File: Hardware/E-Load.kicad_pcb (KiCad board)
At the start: 2 copper layers, 63.5 x 71.1 mm, 53 parts, among them J1 Barrel_Jack, J2 Conn_01x05_Male, J3 Conn_01x08_Male, J4 Screw_Terminal_01x03, Q1 BUK7M45-40EX, SW1 SW_SPST, SW2 SW_Push, SW3 SW_Push, SW4 SW_Push, U1 AP2210K-3.3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

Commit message: Update E-Load.kicad_pcb
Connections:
- U4 pad 6: Net-(D2-Pad1) -> /CurrentControl/ADC
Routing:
- net /CurrentControl/ADC: track 16.6 -> 25.8 mm

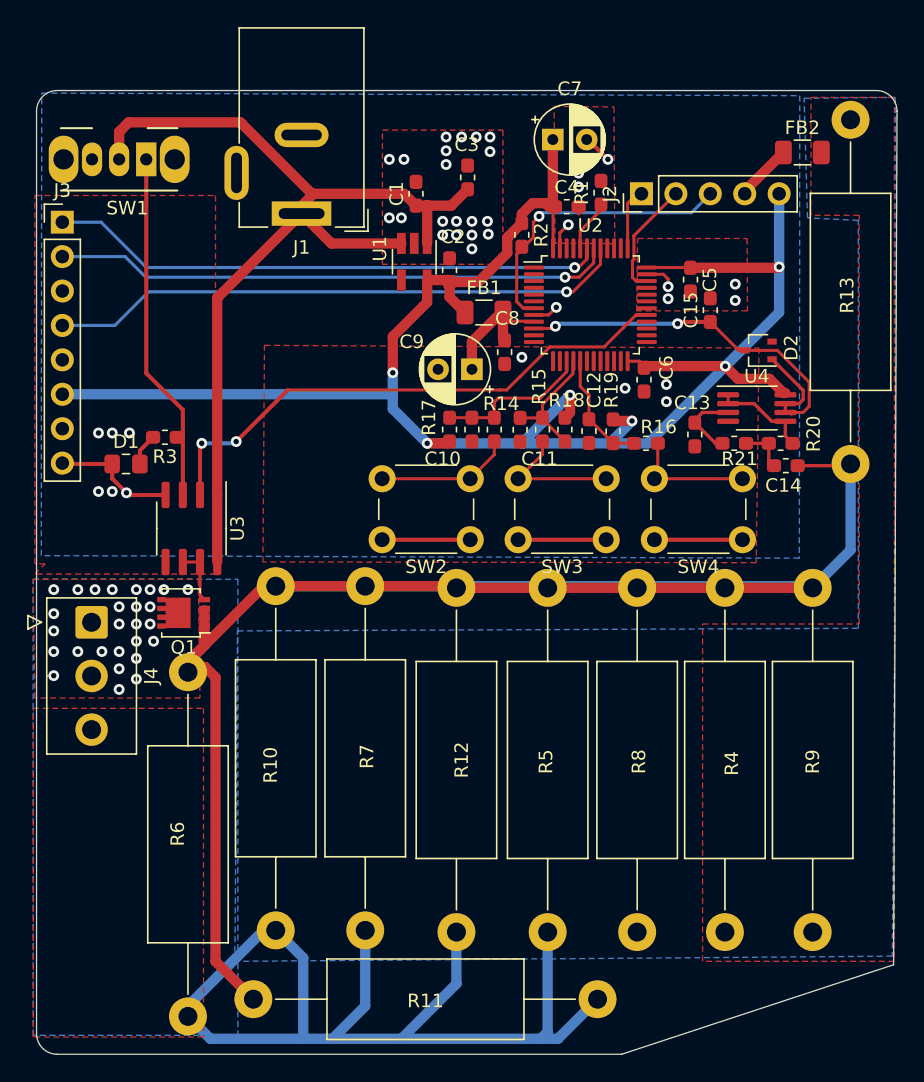
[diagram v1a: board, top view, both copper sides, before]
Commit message: Replaced gate driver with opamp. Replaced feedback circuit with unity gain buffer
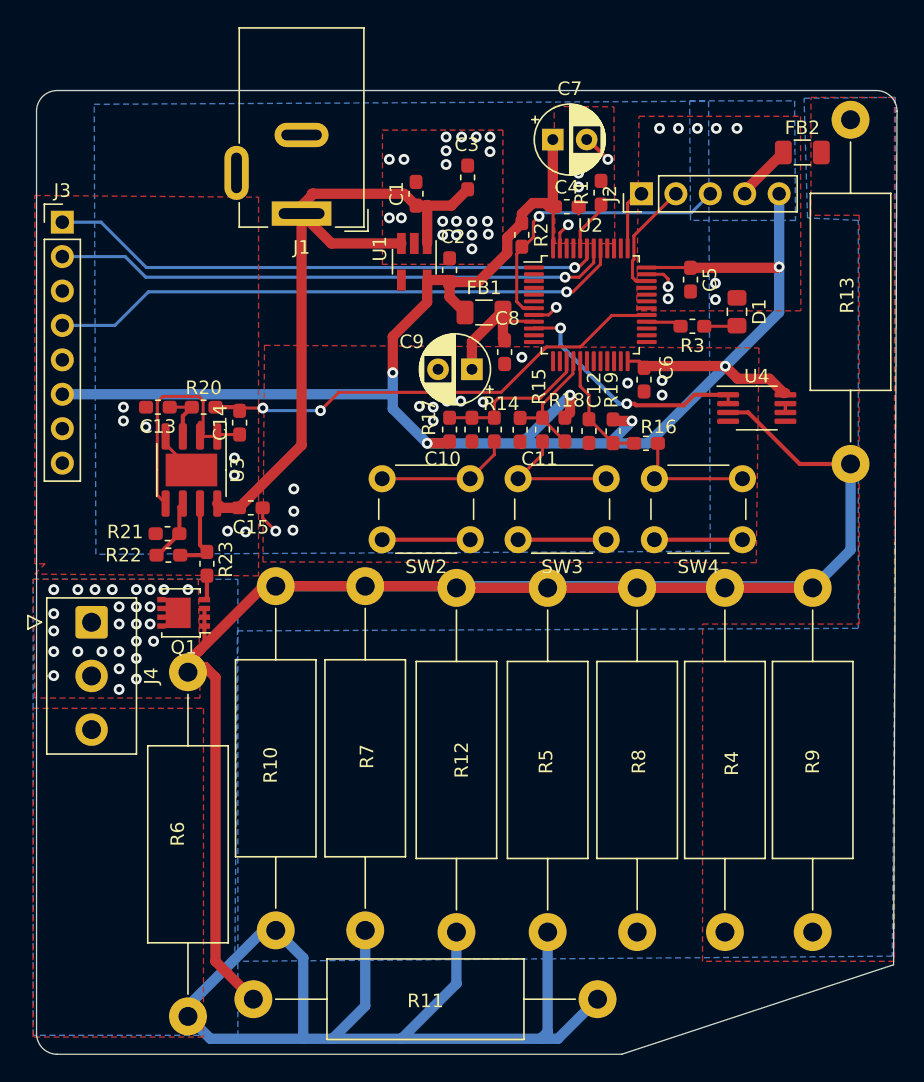
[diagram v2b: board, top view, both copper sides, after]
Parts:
- removed D2: BAT54W, Package_TO_SOT_SMD:SOT-323_SC-70
- removed SW1: SW_SPST, Button_Switch_THT:SW_CuK_OS102011MA1QN1_SPDT_Angled
- added R22: 2.7k, Resistor_SMD:R_0603_1608Metric_Pad1.05x0.95mm_HandSolder, F.Cu at (152.0, 93.7)
- added R23: 15, Resistor_SMD:R_0603_1608Metric_Pad1.05x0.95mm_HandSolder, F.Cu at (154.8, 94.4)
- C15: value 1u -> 100nF
- R20: value 4.32k -> 10.2k
- R21: value 10.2k -> 1k
- R3: value 1K -> 1k
- U3: value MCP14A0302 -> ADA4898-2; footprint Package_SO:SOIC-8_3.9x4.9mm_P1.27mm -> Package_SO:SOIC-8-1EP_3.9x4.9mm_P1.27mm_EP2.41x3.81mm
- moved D1 46.5 mm to (193.9, 75.8), turned to 270 degrees
- moved R20 43.2 mm to (154.6, 82.8)
- moved R21 42.3 mm to (151.9, 92.1)
- moved C14 40.0 mm to (157.2, 83.9), turned to 90 degrees
- moved R3 39.8 mm to (190.6, 76.8)
- moved C13 39.7 mm to (151.2, 82.8), turned to 180 degrees
- moved C15 36.9 mm to (158.1, 90.2), turned to 180 degrees
- moved U3 4.32 mm to (153.7, 87.4)
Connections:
- C14 pad 2: Net-(C14-Pad2) -> /CurrentControl/PWM
- C15 pad 1: /CurrentControl/ADC -> GND
- C15 pad 2: GND -> +12V
- R20 pad 1: Net-(C14-Pad2) -> Net-(C13-Pad1)
- R20 pad 2: /CurrentControl/Vmeas -> /CurrentControl/PWM
- R21 pad 1: Net-(C13-Pad1) -> GND
- R21 pad 2: Net-(C14-Pad2) -> Net-(R21-Pad2)
- R3 pad 1: Net-(R3-Pad1) -> Net-(D1-Pad2)
- R3 pad 2: Net-(D1-Pad2) -> Net-(R3-Pad2)
- U2 pad 28: (no net) -> Net-(R3-Pad2)
- U3 pad 1: +12V -> Net-(C14-Pad1)
- U3 pad 2: /CurrentControl/PWM -> Net-(C14-Pad1)
- U3 pad 3: Net-(R3-Pad1) -> Net-(C13-Pad1)
- U3 pad 5: GND -> Net-(C14-Pad1)
- U3 pad 6: Net-(Q1-Pad4) -> Net-(R21-Pad2)
- U3 pad 7: Net-(Q1-Pad4) -> Net-(R22-Pad1)
- U4 pad 1: Net-(C14-Pad1) -> /CurrentControl/ADC
- U4 pad 2: Net-(C14-Pad1) -> /CurrentControl/ADC
- U4 pad 3: Net-(C13-Pad1) -> /CurrentControl/Vmeas
- U4 pad 5: Net-(C14-Pad1) -> (no net)
- U4 pad 6: /CurrentControl/ADC -> (no net)
- U4 pad 7: Net-(D2-Pad1) -> (no net)
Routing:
- net Net-(R3-Pad1): track 26.4 -> 0.00 mm
- net +12V: track 73.3 -> 51.6 mm
- net Net-(C14-Pad1): track 7.26 -> 18.2 mm
- net /CurrentControl/ADC: track 25.8 -> 18.4 mm
- net Net-(D2-Pad1): track 6.02 -> 0.00 mm
- net Net-(R22-Pad1): track 0.00 -> 5.85 mm
- net /CurrentControl/PWM: track 41.0 -> 35.3 mm
- net /CurrentControl/Vmeas: track 135.4 -> 140.5 mm
- net Net-(R21-Pad2): track 0.00 -> 4.67 mm
- net GND: track 41.8 -> 38.0 mm, vias 39 -> 55
- net Net-(C14-Pad2): track 3.49 -> 0.00 mm
- net Net-(R3-Pad2): track 0.00 -> 2.63 mm
- net Net-(Q1-Pad4): track 4.18 -> 1.84 mm
- net Net-(C13-Pad1): track 5.55 -> 4.06 mm
- net (no net): track 0.00 -> 0.65 mm

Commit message: Changed the PWM control circuit
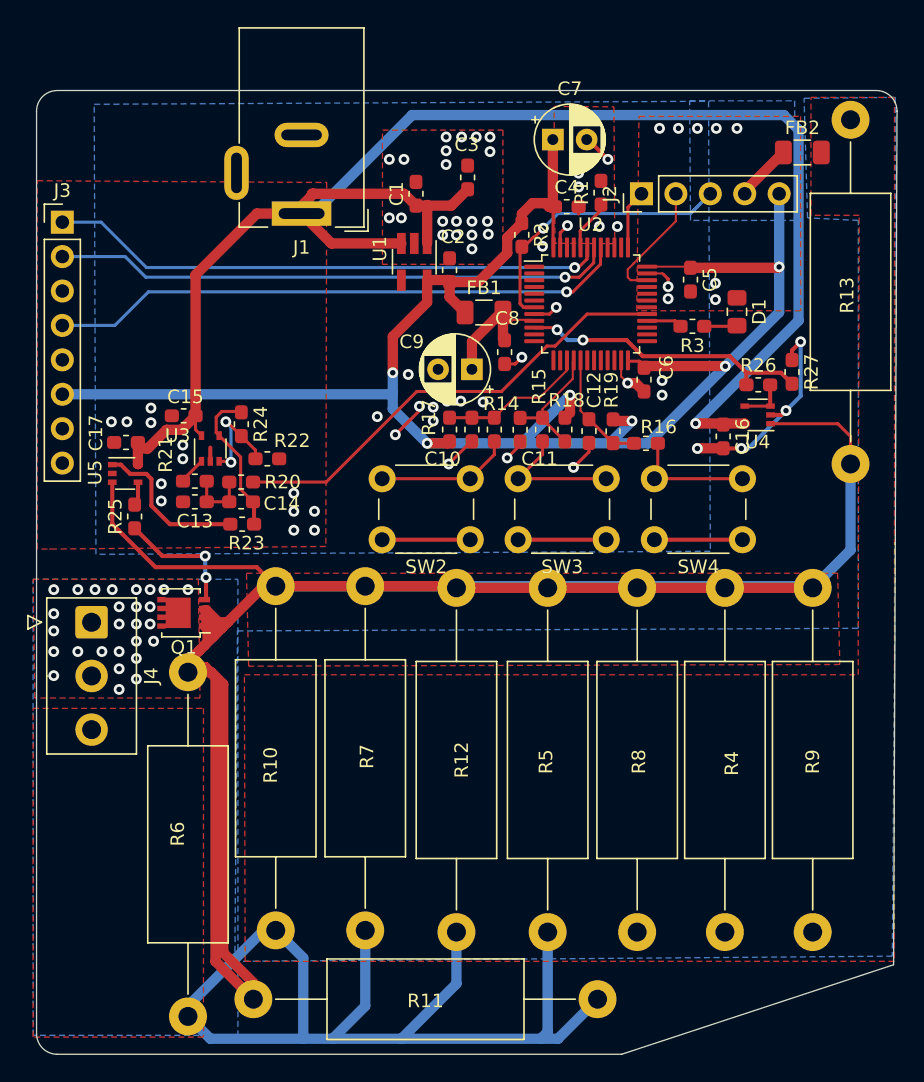
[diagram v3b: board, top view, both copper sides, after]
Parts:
- added C16: 1n, Capacitor_SMD:C_0603_1608Metric_Pad1.05x0.95mm_HandSolder, F.Cu at (192.9, 85.0)
- added C17: 1n, Capacitor_SMD:C_0603_1608Metric_Pad1.05x0.95mm_HandSolder, F.Cu at (148.8, 85.4)
- added R24: 46.4k, Resistor_SMD:R_0603_1608Metric_Pad1.05x0.95mm_HandSolder, F.Cu at (157.4, 84.1)
- added R25: 50, Resistor_SMD:R_0603_1608Metric_Pad1.05x0.95mm_HandSolder, F.Cu at (149.5, 90.9)
- added R26: 20k, Resistor_SMD:R_0603_1608Metric_Pad1.05x0.95mm_HandSolder, F.Cu at (195.5, 81.2)
- added R27: 10k, Resistor_SMD:R_0603_1608Metric_Pad1.05x0.95mm_HandSolder, F.Cu at (198.0, 80.2)
- added U5: TLV172IDCK, Package_TO_SOT_SMD:SOT-353_SC-70-5, F.Cu at (148.8, 87.7)
- C13: value 0.01uF -> 1n
- C14: value 0.082uF -> 470p
- C15: value 100nF -> 1n
- R20: value 10.2k -> 25.5k
- R21: value 1k -> 21k
- R22: value 2.7k -> 23.2k
- R23: value 15 -> 50
- U2: value STM32F102C8Tx -> STM32F103C8Tx
- U3: value ADA4898-2 -> TLV172IDCK; footprint Package_SO:SOIC-8-1EP_3.9x4.9mm_P1.27mm_EP2.41x3.81mm -> Package_TO_SOT_SMD:SOT-353_SC-70-5
- U4: value MCP6L02x-xMS -> TLV172IDCK; footprint Package_SO:MSOP-8_3x3mm_P0.65mm -> Package_TO_SOT_SMD:SOT-353_SC-70-5
- moved R22 10.2 mm to (159.3, 86.6)
- moved C15 8.41 mm to (153.1, 83.4)
- moved C13 7.50 mm to (153.9, 89.8)
- moved R20 6.18 mm to (157.3, 88.3), turned to 180 degrees
- moved C14 5.84 mm to (157.3, 89.8), turned to 180 degrees
- moved R21 4.37 mm to (153.9, 88.3), turned to 180 degrees
- moved R23 3.91 mm to (157.4, 91.4), turned to 0 degrees
- moved U3 2.11 mm to (155.1, 85.9), turned to 90 degrees
- moved U4 0.51 mm to (195.5, 83.4), turned to 180 degrees
- moved U2 0.07 mm to (183.1, 75.2)
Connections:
- C14 pad 2: /CurrentControl/PWM -> Net-(C13-Pad1)
- C15 pad 1: GND -> +12V
- C15 pad 2: +12V -> GND
- R20 pad 1: Net-(C13-Pad1) -> /CurrentControl/PWM
- R20 pad 2: /CurrentControl/PWM -> Net-(C13-Pad1)
- R21 pad 1: GND -> Net-(C13-Pad1)
- R22 pad 1: Net-(R22-Pad1) -> GND
- R22 pad 2: Net-(R21-Pad2) -> Net-(R22-Pad2)
- R23 pad 1: Net-(Q1-Pad4) -> Net-(R23-Pad1)
- R23 pad 2: Net-(R22-Pad1) -> Net-(C14-Pad1)
- U3 pad 1: Net-(C14-Pad1) -> Net-(R21-Pad2)
- U3 pad 2: Net-(C14-Pad1) -> GND
- U3 pad 3: Net-(C13-Pad1) -> Net-(R22-Pad2)
- U3 pad 4: GND -> Net-(C14-Pad1)
- U3 pad 5: Net-(C14-Pad1) -> +12V
- U4 pad 1: /CurrentControl/ADC -> /CurrentControl/Vmeas
- U4 pad 2: /CurrentControl/ADC -> GND
- U4 pad 3: /CurrentControl/Vmeas -> Net-(R26-Pad2)
- U4 pad 4: GND -> Net-(R26-Pad2)
- U4 pad 5: (no net) -> +12V
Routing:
- net +12V: track 51.6 -> 123.0 mm, vias 0 -> 1
- net /CurrentControl/Vmeas: track 140.5 -> 187.1 mm
- net GND: track 38.0 -> 64.0 mm, vias 55 -> 70
- net Net-(R23-Pad1): track 0.00 -> 11.7 mm
- net Net-(R22-Pad2): track 0.00 -> 7.73 mm, vias 0 -> 2
- net Net-(Q1-Pad4): track 1.84 -> 9.34 mm, vias 0 -> 2
- net Net-(C14-Pad1): track 18.2 -> 11.1 mm
- net Net-(R22-Pad1): track 5.85 -> 0.00 mm
- net +3V3: track 139.3 -> 134.0 mm
- net Net-(R26-Pad2): track 0.00 -> 3.48 mm
- net /CurrentControl/ADC: track 18.4 -> 21.8 mm
- net Net-(R21-Pad2): track 4.67 -> 2.03 mm
- net Net-(R25-Pad2): track 0.00 -> 1.75 mm
- net /CurrentControl/PWM: track 35.3 -> 34.2 mm, vias 2 -> 0
- net /MCU/~RST: track 21.8 -> 22.9 mm
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- added copper zone on F.Cu, net /CurrentControl/Vmeas
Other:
- net class Default: clearance 0.2 -> 0.1778
- rule trace_clearance: 0.2 -> 0.1778
- rule trace_min: 0.2 -> 0.127

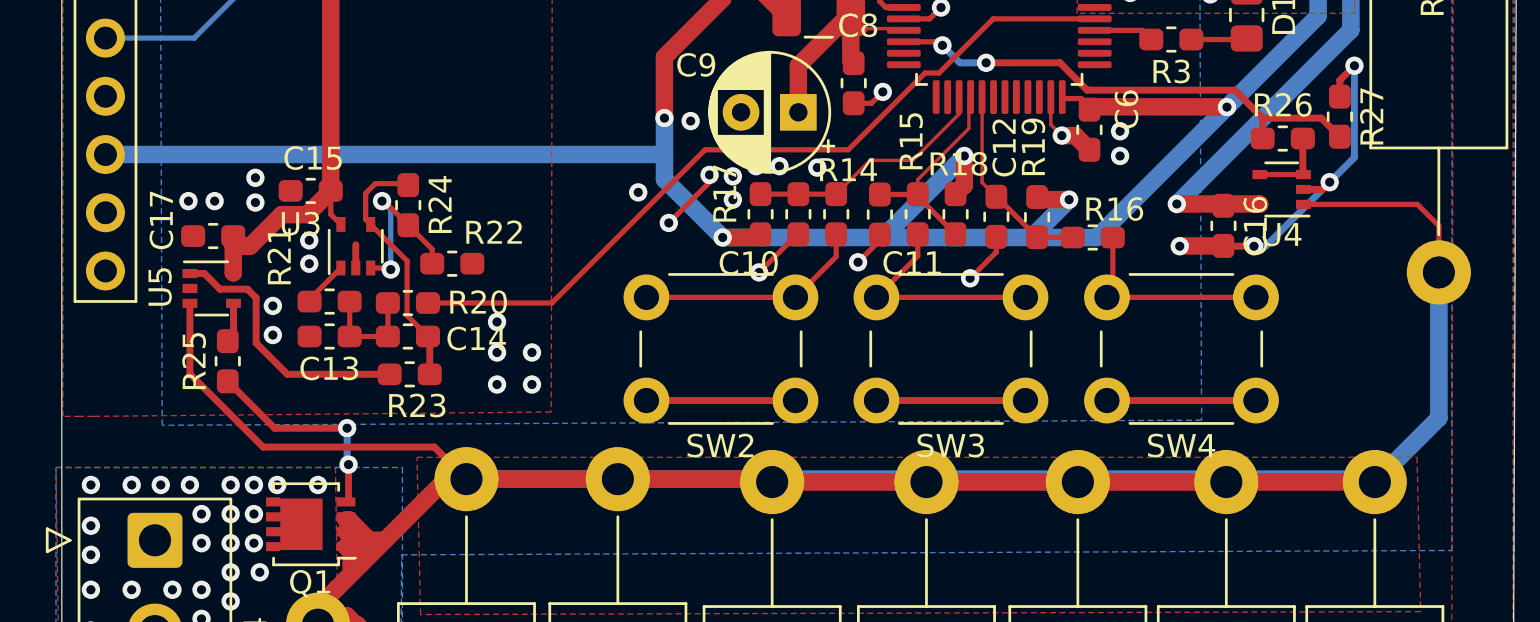
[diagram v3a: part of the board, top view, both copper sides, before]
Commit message: Added Test points
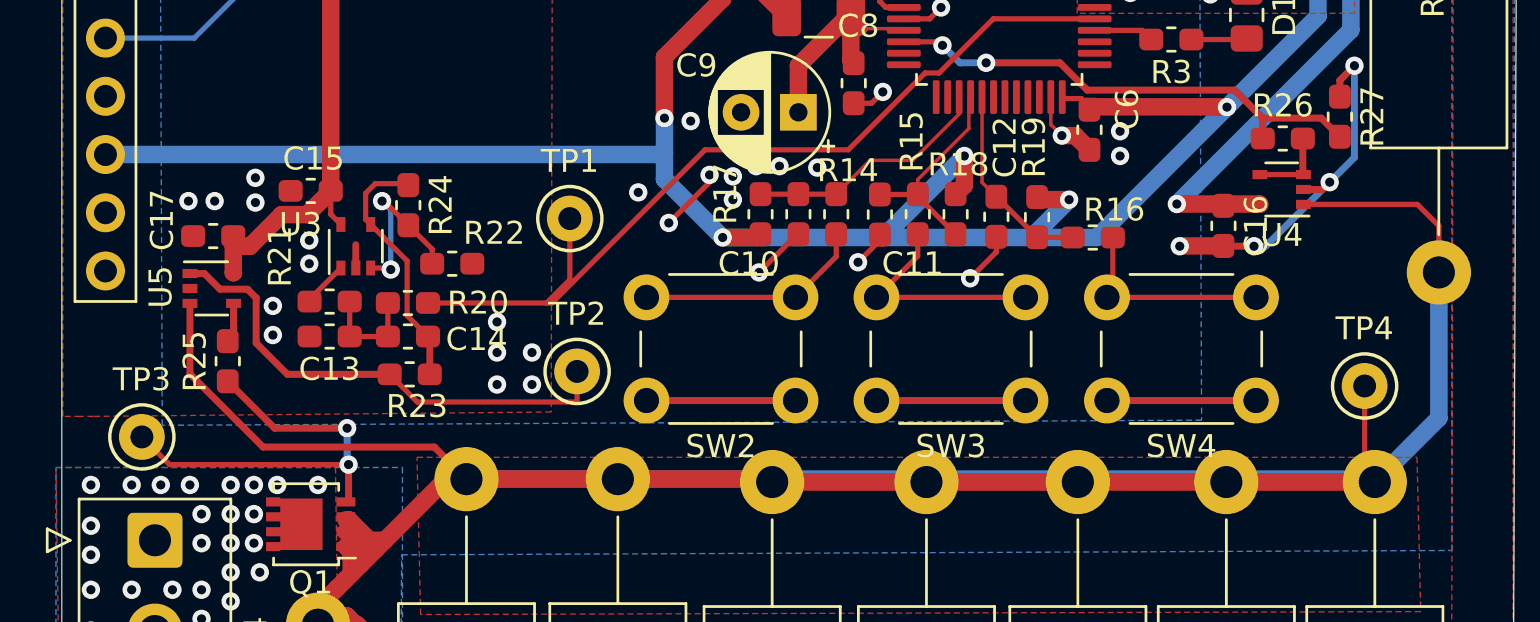
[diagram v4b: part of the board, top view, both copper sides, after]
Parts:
- added TP1: TestPoint_Alt, TestPoint:TestPoint_Keystone_5000-5004_Miniature, F.Cu at (164.4, 84.6)
- added TP2: TestPoint_Alt, TestPoint:TestPoint_Keystone_5000-5004_Miniature, F.Cu at (164.7, 91.3)
- added TP3: TestPoint_Alt, TestPoint:TestPoint_Keystone_5000-5004_Miniature, F.Cu at (145.7, 94.2)
- added TP4: TestPoint_Alt, TestPoint:TestPoint_Keystone_5000-5004_Miniature, F.Cu at (199.1, 91.9)
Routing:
- net Net-(R23-Pad1): track 11.7 -> 21.7 mm
- net Net-(Q1-Pad4): track 9.34 -> 18.9 mm
- net /CurrentControl/Vmeas: track 187.1 -> 191.5 mm
- net /CurrentControl/PWM: track 34.2 -> 38.3 mm
